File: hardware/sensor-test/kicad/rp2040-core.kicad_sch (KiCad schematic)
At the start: 34 parts, among them J1 Conn_02x18_Odd_Even, J2 Conn_01x02, J3 USB_B_Micro, J4 Conn_02x18_Odd_Even, U1 NCP1117-3.3_SOT223, U2 W25Q128JVS, U3 RP2040, Y1 ABLS-12.000MHZ-B4-T

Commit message: Normalize RP2040 core references and exclude legacy hardware
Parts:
- C90: renamed from C2; now left out of the parts list
- C91: renamed from C17; now left out of the parts list
- H90: renamed from H1; now left out of the parts list
- H91: renamed from H2; now left out of the parts list
- H92: renamed from H3; now left out of the parts list
- H93: renamed from H4; now left out of the parts list
- J90: renamed from J3; value USB_B_Micro -> LEGACY_USB_LOGICAL_PLACEHOLDER; now left out of the parts list
- J91: renamed from J1; value Conn_02x18_Odd_Even -> LOGICAL_GPIO_BREAKOUT_NOT_FITTED; now left out of the parts list
- J92: renamed from J4; value Conn_02x18_Odd_Even -> LOGICAL_GPIO_BREAKOUT_NOT_FITTED; now left out of the parts list
- J93: renamed from J2; now left out of the parts list
- U2: value W25Q128JVS -> W25Q16JVUXIQ; footprint Package_SO:SOIC-8_5.23x5.23mm_P1.27mm -> keebio:USON-8_UX_2x3x0p6_WIN; LCSC C97521 -> C2843335
- U90: renamed from U1; now left out of the parts list
- renumbered U3 to U1
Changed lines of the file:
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@@
   (symbol (lib_id "MCU_RaspberryPi_RP2040:RP2040") (at 198.12 144.78 0) (unit 1)
     (in_bom yes) (on_board yes) (dnp no)
-    (property "Reference" "U3" (at 170.18 95.25 0)
+    (property "Reference" "U1" (at 170.18 95.25 0)
       (effects (font (size 1.27 1.27)))
     )
@@
       (project "rp2040-core"
         (path "/0b572f4d-42c2-4e67-a259-3bf815f1855a"
-          (reference "U3") (unit 1)
+          (reference "U1") (unit 1)
         )
       )
@@
       (effects (font (size 1.27 1.27)))
     )
-    (property "Value" "W25Q128JVS" (at 86.36 138.43 0)
-      (effects (font (size 1.27 1.27)))
-    )
-    (property "Footprint" "Package_SO:SOIC-8_5.23x5.23mm_P1.27mm" (at 78.74 128.27 0)
-      (effects (font (size 1.27 1.27)) hide)
-    )
-    (property "Datasheet" "http://www.winbond.com/resource-files/w25q128jv_dtr%20revc%2003272018%20plus.pdf" (at 78.74 128.27 0)
-      (effects (font (size 1.27 1.27)) hide)
-    )
-    (property "LCSC" "C97521" (at 78.74 128.27 0)
+    (property "Value" "W25Q16JVUXIQ" (at 86.36 138.43 0)
+      (effects (font (size 1.27 1.27)))
+    )
+    (property "Footprint" "keebio:USON-8_UX_2x3x0p6_WIN" (at 78.74 128.27 0)
+      (effects (font (size 1.27 1.27)) hide)
+    )
+    (property "Datasheet" "https://www.winbond.com/hq/product/code-storage-flash-memory/serial-nor-flash/?__locale=en&partNo=W25Q16JV" (at 78.74 128.27 0)
+      (effects (font (size 1.27 1.27)) hide)
+    )
+    (property "LCSC" "C2843335" (at 78.74 128.27 0)
       (effects (font (size 1.27 1.27)) hide)
     )
@@
   )
   (symbol (lib_id "RP2040_minimal-rescue:USB_B_Micro-Connector") (at 33.02 49.53 0) (unit 1)
-    (in_bom yes) (on_board yes) (dnp no)
-    (property "Reference" "J3" (at 29.21 39.37 0)
+    (in_bom no) (on_board no) (dnp no)
+    (property "Reference" "J90" (at 29.21 39.37 0)
       (effects (font (size 1.27 1.27)) (justify right))
     )
-    (property "Value" "USB_B_Micro" (at 46.99 59.69 0)
+    (property "Value" "LEGACY_USB_LOGICAL_PLACEHOLDER" (at 46.99 59.69 0)
       (effects (font (size 1.27 1.27)) (justify right))
     )
@@
       (project "rp2040-core"
         (path "/0b572f4d-42c2-4e67-a259-3bf815f1855a"
-          (reference "J3") (unit 1)
+          (reference "J90") (unit 1)
         )
       )
@@
   )
   (symbol (lib_id "Mechanical:MountingHole") (at 251.46 259.08 0) (unit 1)
-    (in_bom yes) (on_board yes) (dnp no)
-    (property "Reference" "H1" (at 254 257.9116 0)
+    (in_bom no) (on_board no) (dnp no)
+    (property "Reference" "H90" (at 254 257.9116 0)
       (effects (font (size 1.27 1.27)) (justify left))
     )
@@
       (project "rp2040-core"
         (path "/0b572f4d-42c2-4e67-a259-3bf815f1855a"
-          (reference "H1") (unit 1)
+          (reference "H90") (unit 1)
         )
       )
@@
   )
   (symbol (lib_id "Mechanical:MountingHole") (at 251.46 264.16 0) (unit 1)
-    (in_bom yes) (on_board yes) (dnp no)
-    (property "Reference" "H2" (at 254 262.9916 0)
+    (in_bom no) (on_board no) (dnp no)
+    (property "Reference" "H91" (at 254 262.9916 0)
       (effects (font (size 1.27 1.27)) (justify left))
     )
@@
       (project "rp2040-core"
         (path "/0b572f4d-42c2-4e67-a259-3bf815f1855a"
-          (reference "H2") (unit 1)
+          (reference "H91") (unit 1)
         )
       )
@@
   )
   (symbol (lib_id "Mechanical:MountingHole") (at 251.46 269.24 0) (unit 1)
-    (in_bom yes) (on_board yes) (dnp no)
-    (property "Reference" "H4" (at 254 268.0716 0)
+    (in_bom no) (on_board no) (dnp no)
+    (property "Reference" "H93" (at 254 268.0716 0)
       (effects (font (size 1.27 1.27)) (justify left))
     )
@@
       (project "rp2040-core"
         (path "/0b572f4d-42c2-4e67-a259-3bf815f1855a"
-          (reference "H4") (unit 1)
+          (reference "H93") (unit 1)
         )
       )
@@
   )
   (symbol (lib_id "Mechanical:MountingHole") (at 251.46 274.32 0) (unit 1)
-    (in_bom yes) (on_board yes) (dnp no)
-    (property "Reference" "H3" (at 254 273.1516 0)
+    (in_bom no) (on_board no) (dnp no)
+    (property "Reference" "H92" (at 254 273.1516 0)
       (effects (font (size 1.27 1.27)) (justify left))
     )
@@
       (project "rp2040-core"
         (path "/0b572f4d-42c2-4e67-a259-3bf815f1855a"
-          (reference "H3") (unit 1)
+          (reference "H92") (unit 1)
         )
       )
@@
   )
   (symbol (lib_id "Regulator_Linear:NCP1117-3.3_SOT223") (at 76.2 44.45 0) (unit 1)
-    (in_bom yes) (on_board yes) (dnp no)
-    (property "Reference" "U1" (at 76.2 38.3032 0)
+    (in_bom no) (on_board no) (dnp no)
+    (property "Reference" "U90" (at 76.2 38.3032 0)
       (effects (font (size 1.27 1.27)))
     )
@@
       (project "rp2040-core"
         (path "/0b572f4d-42c2-4e67-a259-3bf815f1855a"
-          (reference "U1") (unit 1)
+          (reference "U90") (unit 1)
         )
       )
@@
   )
   (symbol (lib_id "Device:C") (at 58.42 49.53 0) (unit 1)
-    (in_bom yes) (on_board yes) (dnp no)
-    (property "Reference" "C2" (at 61.341 48.3616 0)
+    (in_bom no) (on_board no) (dnp no)
+    (property "Reference" "C90" (at 61.341 48.3616 0)
       (effects (font (size 1.27 1.27)) (justify left))
     )
@@
       (project "rp2040-core"
         (path "/0b572f4d-42c2-4e67-a259-3bf815f1855a"
-          (reference "C2") (unit 1)
+          (reference "C90") (unit 1)
         )
       )
@@
   )
   (symbol (lib_id "Device:C") (at 93.98 49.53 0) (unit 1)
-    (in_bom yes) (on_board yes) (dnp no)
-    (property "Reference" "C17" (at 96.901 48.3616 0)
+    (in_bom no) (on_board no) (dnp no)
+    (property "Reference" "C91" (at 96.901 48.3616 0)
       (effects (font (size 1.27 1.27)) (justify left))
     )
@@
       (project "rp2040-core"
         (path "/0b572f4d-42c2-4e67-a259-3bf815f1855a"
-          (reference "C17") (unit 1)
+          (reference "C91") (unit 1)
         )
       )
@@
   )
   (symbol (lib_id "Connector_Generic:Conn_01x02") (at 26.67 125.73 0) (mirror y) (unit 1)
-    (in_bom yes) (on_board yes) (dnp no)
-    (property "Reference" "J2" (at 25.4 121.92 0)
+    (in_bom no) (on_board no) (dnp no)
+    (property "Reference" "J93" (at 25.4 121.92 0)
       (effects (font (size 1.27 1.27)))
     )
@@
       (project "rp2040-core"
         (path "/0b572f4d-42c2-4e67-a259-3bf815f1855a"
-          (reference "J2") (unit 1)
+          (reference "J93") (unit 1)
         )
       )
@@
   )
   (symbol (lib_id "Connector_Generic:Conn_02x18_Odd_Even") (at 375.92 142.24 0) (unit 1)
-    (in_bom yes) (on_board yes) (dnp no)
-    (property "Reference" "J4" (at 377.19 116.4082 0)
-      (effects (font (size 1.27 1.27)))
-    )
-    (property "Value" "Conn_02x18_Odd_Even" (at 377.19 118.7196 0)
+    (in_bom no) (on_board no) (dnp no)
+    (property "Reference" "J92" (at 377.19 116.4082 0)
+      (effects (font (size 1.27 1.27)))
+    )
+    (property "Value" "LOGICAL_GPIO_BREAKOUT_NOT_FITTED" (at 377.19 118.7196 0)
       (effects (font (size 1.27 1.27)))
     )
@@
       (project "rp2040-core"
         (path "/0b572f4d-42c2-4e67-a259-3bf815f1855a"
-          (reference "J4") (unit 1)
+          (reference "J92") (unit 1)
         )
       )
@@
   )
   (symbol (lib_id "Connector_Generic:Conn_02x18_Odd_Even") (at 318.77 142.24 0) (unit 1)
-    (in_bom yes) (on_board yes) (dnp no)
-    (property "Reference" "J1" (at 320.04 116.4082 0)
-      (effects (font (size 1.27 1.27)))
-    )
-    (property "Value" "Conn_02x18_Odd_Even" (at 320.04 118.7196 0)
+    (in_bom no) (on_board no) (dnp no)
+    (property "Reference" "J91" (at 320.04 116.4082 0)
+      (effects (font (size 1.27 1.27)))
+    )
+    (property "Value" "LOGICAL_GPIO_BREAKOUT_NOT_FITTED" (at 320.04 118.7196 0)
       (effects (font (size 1.27 1.27)))
     )
@@
       (project "rp2040-core"
         (path "/0b572f4d-42c2-4e67-a259-3bf815f1855a"
-          (reference "J1") (unit 1)
-        )
-      )
+          (reference "J91") (unit 1)
+        )
+      )

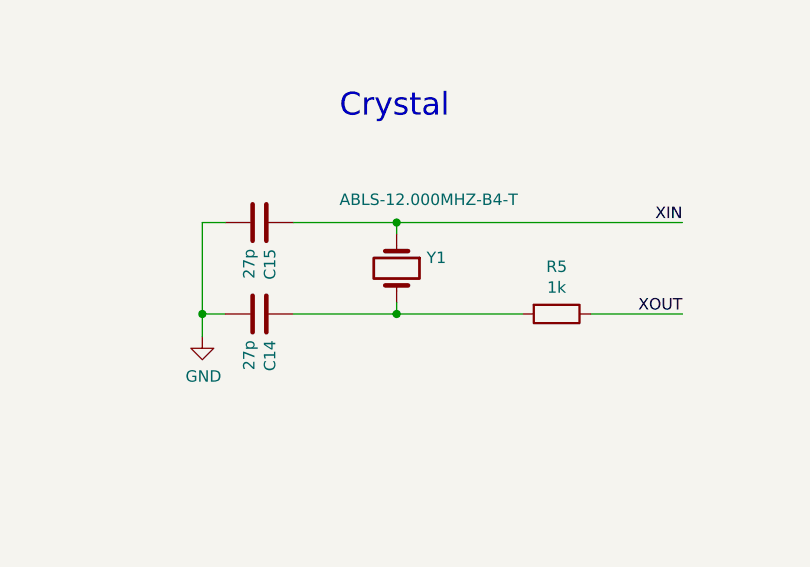
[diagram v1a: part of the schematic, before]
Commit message: Use recommended ABM8 RP2040 crystal network
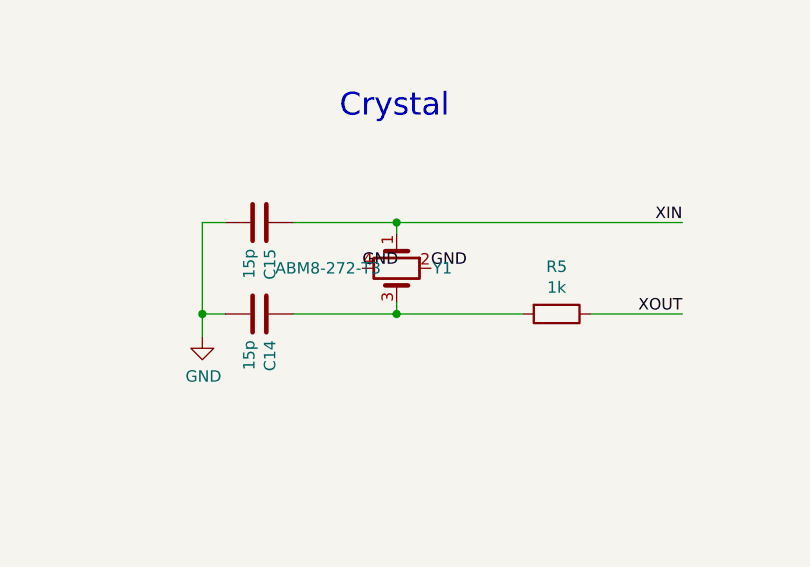
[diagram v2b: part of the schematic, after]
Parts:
- C14, C15: value 27p -> 15p; LCSC C52923 -> (none)
- Y1: value ABLS-12.000MHZ-B4-T -> ABM8-272-T3; footprint RP2040_minimal:Crystal_SMD_HC49-US -> Crystal:Crystal_SMD_3225-4Pin_3.2x2.5mm; symbol Device:Crystal -> HEP:ABM8-272-T3; LCSC C110563 -> (none)
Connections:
- net GND: now also Y1.2 (GND), Y1.4 (GND)
- net at C14.1, R5.2: now also Y1.3 (XTAL2); no longer Y1.2
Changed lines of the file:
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@@
       (effects (font (size 1.27 1.27)) (justify left))
     )
-    (property "Value" "27p" (at 49.657 221.361 0)
+    (property "Value" "15p" (at 49.657 221.361 0)
       (effects (font (size 1.27 1.27)) (justify left))
     )
@@
       (effects (font (size 1.27 1.27)) hide)
     )
-    (property "Datasheet" "https://datasheet.lcsc.com/lcsc/1811091611_Samsung-Electro-Mechanics-CL05A105KA5NQNC_C52923.pdf" (at 50.8 218.44 0)
-      (effects (font (size 1.27 1.27)) hide)
-    )
-    (property "LCSC" "C52923" (at 50.8 218.44 0)
+    (property "Datasheet" "~" (at 50.8 218.44 0)
+      (effects (font (size 1.27 1.27)) hide)
+    )
+    (property "LCSC" "" (at 50.8 218.44 0)
       (effects (font (size 1.27 1.27)) hide)
     )
@@
       (effects (font (size 1.27 1.27)) (justify left))
     )
-    (property "Value" "27p" (at 49.657 231.521 0)
+    (property "Value" "15p" (at 49.657 231.521 0)
       (effects (font (size 1.27 1.27)) (justify left))
     )
@@
       (effects (font (size 1.27 1.27)) hide)
     )
-    (property "Datasheet" "https://datasheet.lcsc.com/lcsc/1811091611_Samsung-Electro-Mechanics-CL05A105KA5NQNC_C52923.pdf" (at 50.8 228.6 0)
-      (effects (font (size 1.27 1.27)) hide)
-    )
-    (property "LCSC" "C52923" (at 50.8 228.6 0)
+    (property "Datasheet" "~" (at 50.8 228.6 0)
+      (effects (font (size 1.27 1.27)) hide)
+    )
+    (property "LCSC" "" (at 50.8 228.6 0)
       (effects (font (size 1.27 1.27)) hide)
     )
@@
     )
   )
-  (symbol (lib_id "Device:Crystal") (at 66.04 223.52 270) (unit 1)
-    (in_bom yes) (on_board yes) (dnp no)
-    (property "Reference" "Y1" (at 69.3674 222.3516 90)
-      (effects (font (size 1.27 1.27)) (justify left))
-    )
-    (property "Value" "ABLS-12.000MHZ-B4-T" (at 59.69 215.9 90)
-      (effects (font (size 1.27 1.27)) (justify left))
-    )
-    (property "Footprint" "RP2040_minimal:Crystal_SMD_HC49-US" (at 66.04 223.52 0)
-      (effects (font (size 1.27 1.27)) hide)
-    )
-    (property "Datasheet" "https://datasheet.lcsc.com/lcsc/2103291134_Yangxing-Tech-X49SM12MSB2SC_C110563.pdf" (at 66.04 223.52 0)
-      (effects (font (size 1.27 1.27)) hide)
-    )
-    (property "LCSC" "C110563" (at 66.04 223.52 0)
-      (effects (font (size 1.27 1.27)) hide)
-    )
-    (pin "1")
-    (pin "2")
+  (symbol (lib_id "HEP:ABM8-272-T3") (at 66.04 223.52 270) (unit 1)
+    (in_bom yes) (on_board yes) (dnp no)
+    (property "Reference" "Y1" (at 71.12 223.52 90) (effects (font (size 1.27 1.27))))
+    (property "Value" "ABM8-272-T3" (at 58.42 223.52 90) (effects (font (size 1.27 1.27))))
+    (property "Footprint" "Crystal:Crystal_SMD_3225-4Pin_3.2x2.5mm" (at 66.04 223.52 0) (effects (font (size 1.27 1.27)) hide))
+    (property "Datasheet" "https://abracon.com/Resonators/ABM8-272-T3.pdf" (at 66.04 223.52 0) (effects (font (size 1.27 1.27)) hide))
+    (property "LCSC" "" (at 66.04 223.52 0) (effects (font (size 1.27 1.27)) hide))
+    (pin "1")
+    (pin "2")
+    (pin "3")
+    (pin "4")
     (instances
       (project "rp2040-core"
@@
     )
   )
+  (label "GND" (at 62.23 223.52 0)
+    (effects (font (size 1.27 1.27)) (justify left bottom))
+  )
+  (label "GND" (at 69.85 223.52 0)
+    (effects (font (size 1.27 1.27)) (justify left bottom))
+  )
   (sheet_instances

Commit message: Remove legacy USB/LDO path from RP2040 core
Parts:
- removed C90, C91: 10u, Capacitor_SMD:C_0805_2012Metric, symbol Device:C
- removed J90: LEGACY_USB_LOGICAL_PLACEHOLDER, RP2040_minimal:USB_Micro-B_Amphenol_10103594-0001LF_Horizontal_modified, symbol RP2040_minimal-rescue:USB_B_Micro-Connector
- removed U90: NCP1117-3.3_SOT223, Package_TO_SOT_SMD:SOT-223-3_TabPin2, symbol Regulator_Linear:NCP1117-3.3_SOT223
- added X2: External 3V3 from USB power sheet, symbol HEP:External3V3
- R3, R4, R5: footprint Capacitor_SMD:C_0402_1005Metric -> Resistor_SMD:R_0603_1608Metric
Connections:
- net +3V3: now also X2.1 (3V3_OUT)
- net USB_D+ renamed USB_D+_PROTECTED
- net USB_D- renamed USB_D-_PROTECTED
- no-connect marks 1 -> 0
